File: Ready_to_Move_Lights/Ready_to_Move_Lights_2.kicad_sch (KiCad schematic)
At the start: 30 parts, among them J1 PET-02-XX-X-VT-LC, K1 VORA1150-X017T, Q1 BC107, U1 LM393LVQDDFRQ1, U2 IPBT-102-H1-XX-S-RA, U3 NE555D, U4 IPBT-102-H1-XX-S-RA

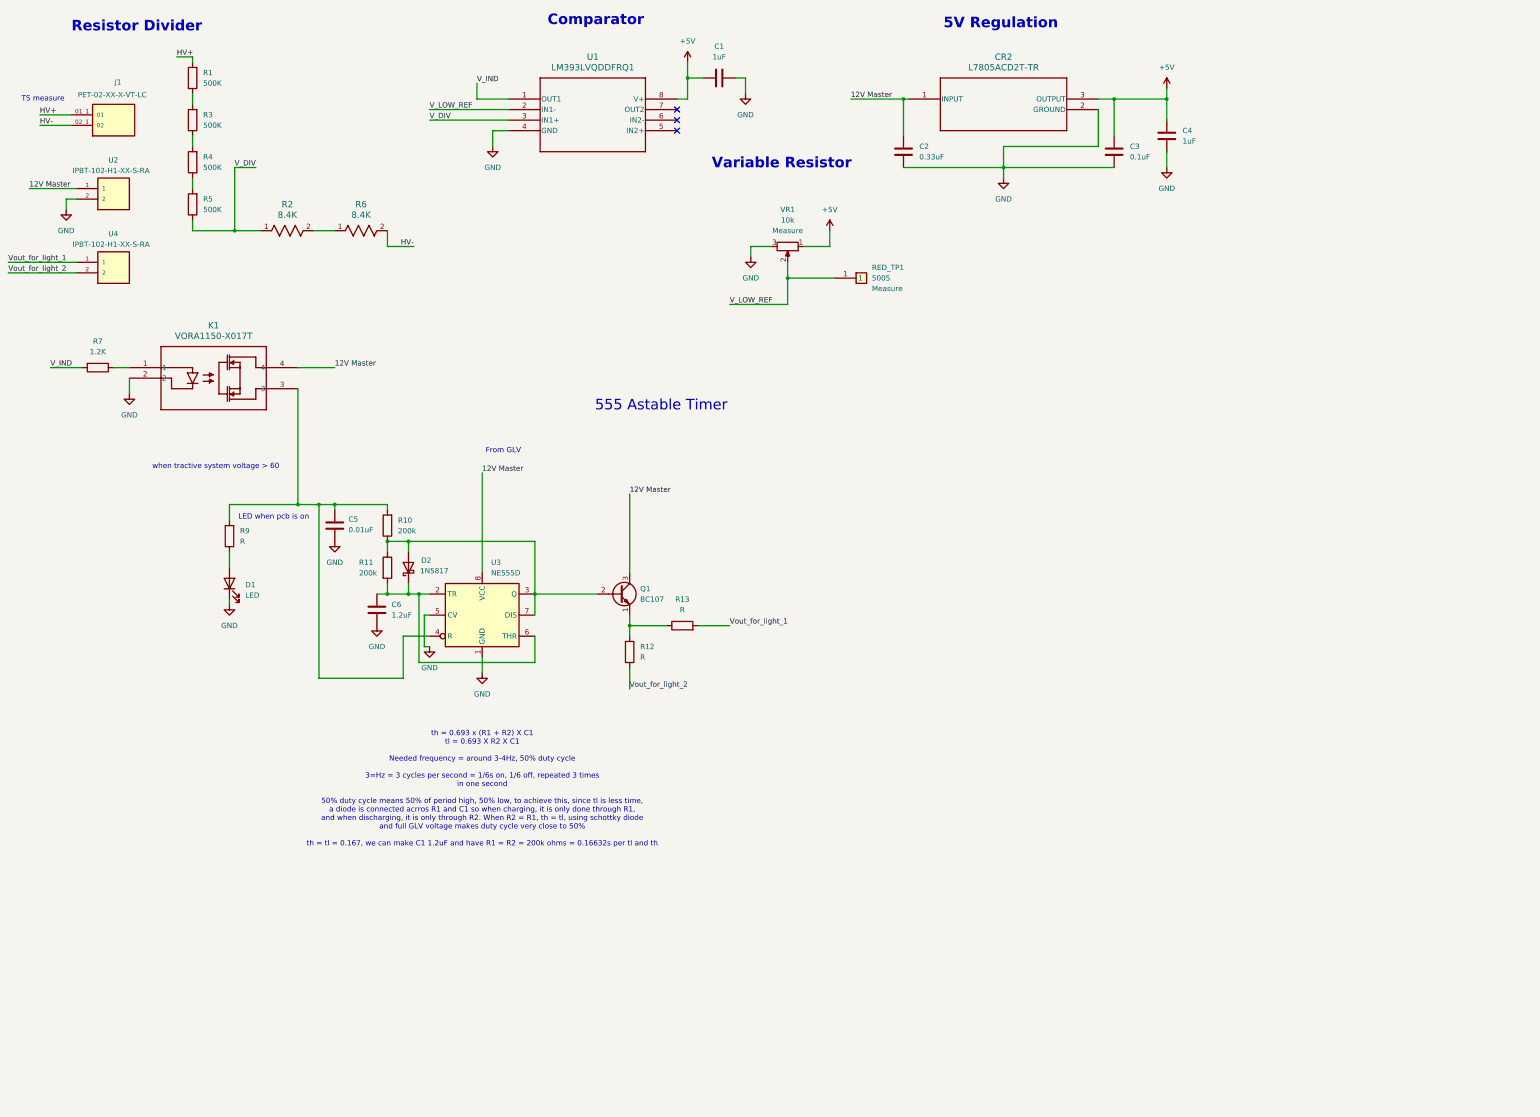
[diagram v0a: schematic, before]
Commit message: Ready_to_Move_Lights
Updated ready to move lights schematic and pcb
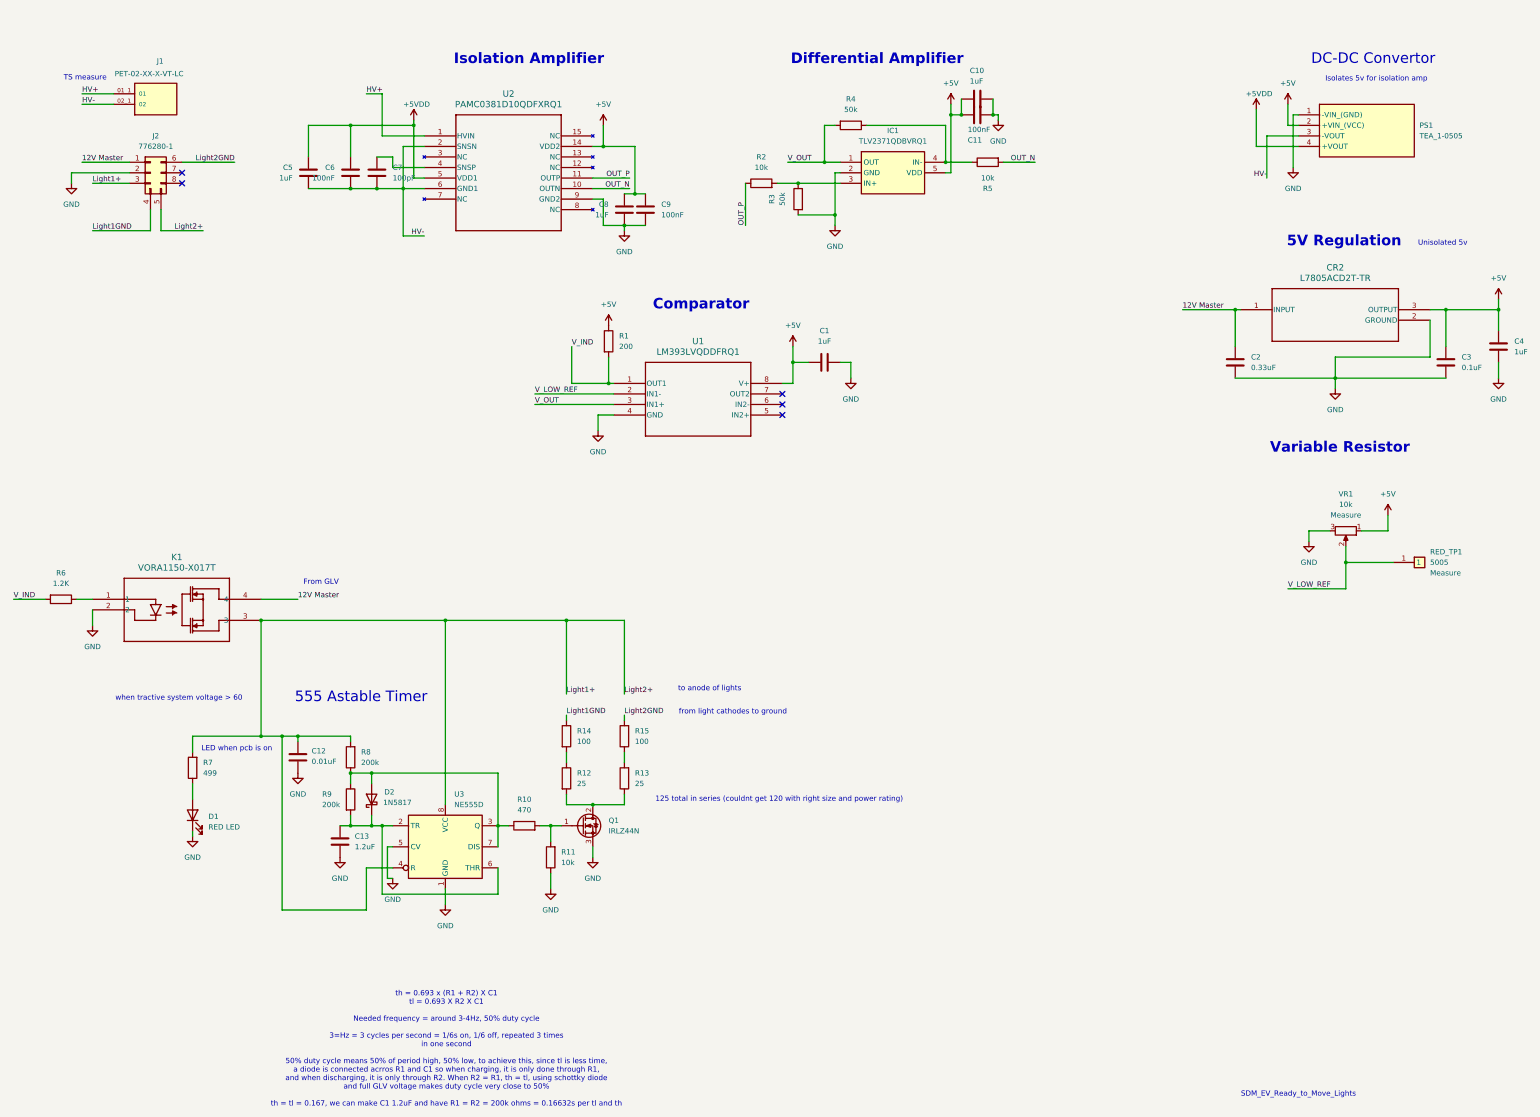
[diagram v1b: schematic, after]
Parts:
- removed Q1: BC107, Package_TO_SOT_THT:TO-18-3, symbol Transistor_BJT:BC107
- removed R2, R6: 8.4K, SDM_MiscFootprint:C_0402_1005Metric, symbol Schematic_Symbols:ERA-2ARB102X
- removed U2, U4: IPBT-102-H1-XX-S-RA, Footprints:IPBT-102-H1-XX-S-RA, symbol Schematic_Symbols:IPBT-102-H1-XX-S-RA
- added C10, C5, C8: 1uF, Capacitor_SMD:C_0603_1608Metric, symbol Device:C
- added C11, C6, C9: 100nF, Capacitor_SMD:C_0603_1608Metric, symbol Device:C
- added C7: 100pF, Capacitor_SMD:C_0603_1608Metric, symbol Device:C
- added IC1: TLV2371QDBVRQ1, Footprints:SOT95P280X145-5N, symbol Schematic_Symbols:TLV2371QDBVRQ1
- added J2: 776280-1, SDM_MiscFootprint:776280-1, symbol SDM_CONNECTOR:776280-1
- added PS1: TEA_1-0505, Footprints:TEA10505, symbol Schematic_Symbols:TEA_1-0505
- added Q1: IRLZ44N, Package_TO_SOT_THT:TO-220-3_Vertical, symbol Transistor_FET:IRLZ44N
- added R10: 470, Resistor_SMD:R_0603_1608Metric, symbol Device:R
- added R11, R2: 10k, Resistor_SMD:R_0603_1608Metric, symbol Device:R
- added R14, R15: 100, Resistor_SMD:R_0603_1608Metric, symbol Device:R
- added U2: PAMC0381D10QDFXRQ1, Footprints:SSOP15_DFX_TEX, symbol Schematic_Symbols:PAMC0381D10QDFXRQ1
- C12: renamed from C5; footprint Capacitor_SMD:C_0603_1608Metric -> Capacitor_SMD:C_0805_2012Metric
- D1: value LED -> RED LED
- R1: value 500K -> 200; footprint Resistor_SMD:R_1206_3216Metric -> Resistor_SMD:R_0603_1608Metric
- R12, R13: value R -> 25
- R3, R4: value 500K -> 50k; footprint Resistor_SMD:R_1206_3216Metric -> Resistor_SMD:R_0603_1608Metric
- R5: value 500K -> 10k; footprint Resistor_SMD:R_1206_3216Metric -> Resistor_SMD:R_0603_1608Metric
- R7: renamed from R9; value R -> 499; footprint Resistor_SMD:R_0603_1608Metric -> Resistor_SMD:R_1206_3216Metric
- renumbered C6 to C13, R7 to R6, R10 to R8, R11 to R9
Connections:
- net Vout_for_light_2 is gone; now on an unnamed net: R12.2
- net +5V: now also R1.1, C10.2, C11.2, C8.2, C9.2, IC1.5 (VDD), PS1.2 (+VIN_(VCC)), U2.14 (VDD2)
- net 01: now also U2.1 (HVIN); no longer R1.2
- net 02: now also C5.1, C6.1, C7.1, PS1.3 (-VOUT), U2.2 (SNSN), U2.6 (GND1)
- net 12V Master: now also J2.1 (Pin_1); no longer U3.8 (VCC)
- net GND: now also R3.2, C10.1, C11.1, C8.1, C9.1, IC1.2 (GND), J2.2 (Pin_2), PS1.1 (-VIN_(GND)), Q1.3 (S), R11.1, U2.9 (GND2)
- net V_IND: now also R1.2
- net at R13.1: now also Q1.2 (D); no longer R12.1
- net at D2.2 (A), R8.1, R9.1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: now also R10.1
- net Light1+: now reaches C12.1, K1.3, R7.2, R8.2, U3.4 (R)
- net Light1+: now also U3.8 (VCC), J2.3 (Pin_3), J2.5 (Pin_5)
- net at R3.1: now also IC1.3 (IN+), R2.2; no longer R4.2
- net at R4.1: now also R5.1, IC1.4 (IN-); no longer R5.2
- net V_DIV renamed V_OUT
- net V_OUT: now also R4.2, IC1.1 (OUT); no longer R5.1
- net Vout_for_light_1: no longer names the net of R13.2
- net Vout_for_light_1: now also R15.1
- new net: Q1.1 (G), R10.2, R11.2
- new net: C7.2, U2.4 (SNSP)
- new net: R12.1, R14.2
- new net +5VDD: C5.2, C6.2, PS1.4 (+VOUT), U2.5 (VDD1)
- new net Light1GND: J2.4 (Pin_4), R14.1
- new net Light2GND: J2.6 (Pin_6), R15.2
- new net OUT_N: R5.2, U2.10 (OUTN)
- new net OUT_P: R2.1, U2.11 (OUTP)
- no-connect marks 3 -> 5
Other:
- note added: "125 total in series (couldnt get 120 with right size and power rating)"
- note added: "DC-DC Convertor"
- note added: "Differential Amplifier"
- note added: "Isolates 5v for isolation amp"
- note added: "Isolation Amplifier"
- note added: "SDM_EV_Ready_to_Move_Lights"
- note added: "Unisolated 5v"
- note added: "from light cathodes to ground"
- note added: "to anode of lights"
- note removed: "Resistor Divider"
- moved on the sheet: C1, C12, C13, C2, C3, C4, CR2, D1, D2, J1, K1, R12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
